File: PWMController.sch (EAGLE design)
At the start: 13 parts, among them IC1 LM555_DIP, Q1 BC337-25

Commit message: Adding updated files
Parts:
- D1, D2: value 1N4148 -> 1N4148DO35-7; device diode-1:1N4148 -> diode:1N4148DO35-7
- D3: device SparkFun-LED:LED5MM -> led:LED5MM
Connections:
- net GND: now also J1.2; no longer J1.1
- net N$1: now also J3.1; no longer J3.3
- net N$4: now also J3.3; no longer J3.1
- net VCC: now also J1.1; no longer J1.2
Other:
- moved on the sheet: J3
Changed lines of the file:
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@@
 <parts>
 <part name="C1" library="rcl" library_urn="urn:adsk.eagle:library:334" deviceset="CPOL-EU" device="E1.8-4" package3d_urn="urn:adsk.eagle:package:23336/2" value="2.2uF"/>
-<part name="IC1" library="IC_Clock-Timing" library_urn="urn:adsk.eagle:library:18568598" deviceset="*555" device="_DIP" package3d_urn="urn:adsk.eagle:package:18493555/1" technology="LM"/>
-<part name="D1" library="diode-1" deviceset="1N4148" device=""/>
-<part name="D2" library="diode-1" deviceset="1N4148" device=""/>
-<part name="D3" library="SparkFun-LED" library_urn="urn:adsk.eagle:library:529" deviceset="LED" device="5MM" package3d_urn="urn:adsk.eagle:package:39353/1"/>
+<part name="IC1" library="IC_Clock-Timing" library_urn="urn:adsk.eagle:library:18568598" deviceset="*555" device="_DIP" package3d_urn="urn:adsk.eagle:package:18493555/1" override_package3d_urn="urn:adsk.eagle:package:23438638/2" override_package_urn="urn:adsk.eagle:footprint:18493706/1" technology="LM"/>
+<part name="D1" library="diode" library_urn="urn:adsk.eagle:library:210" deviceset="1N4148" device="DO35-7" package3d_urn="urn:adsk.eagle:package:43339/2"/>
+<part name="D2" library="diode" library_urn="urn:adsk.eagle:library:210" deviceset="1N4148" device="DO35-7" package3d_urn="urn:adsk.eagle:package:43339/2"/>
+<part name="D3" library="led" library_urn="urn:adsk.eagle:library:259" deviceset="LED" device="5MM" package3d_urn="urn:adsk.eagle:package:15799/2"/>
 <part name="R2" library="rcl" library_urn="urn:adsk.eagle:library:334" deviceset="R-EU_" device="R1206" package3d_urn="urn:adsk.eagle:package:23540/2"/>
 <part name="C2" library="Capacitor" library_urn="urn:adsk.eagle:library:16290819" deviceset="C" device="CHIP-1206(3216-METRIC)" package3d_urn="urn:adsk.eagle:package:16290893/2" technology="_" value="10nF"/>
@@
 <attribute name="VALUE" x="185.42" y="71.12" size="1.778" layer="96"/>
 </instance>
-<instance part="GND2" gate="1" x="213.36" y="99.06" smashed="yes" grouprefs="POWER_TERMINALS">
-<attribute name="VALUE" x="210.82" y="96.52" size="1.778" layer="96"/>
-</instance>
-<instance part="P+2" gate="1" x="215.9" y="101.6" smashed="yes" rot="R180" grouprefs="POWER_TERMINALS">
-<attribute name="VALUE" x="218.44" y="101.6" size="1.778" layer="96"/>
+<instance part="GND2" gate="1" x="213.36" y="93.98" smashed="yes" grouprefs="POWER_TERMINALS">
+<attribute name="VALUE" x="210.82" y="91.44" size="1.778" layer="96"/>
+</instance>
+<instance part="P+2" gate="1" x="215.9" y="96.52" smashed="yes" rot="R180" grouprefs="POWER_TERMINALS">
+<attribute name="VALUE" x="218.44" y="96.52" size="1.778" layer="96"/>
 </instance>
 <instance part="P+1" gate="VCC" x="187.96" y="111.76" smashed="yes" grouprefs="POWER_TERMINALS">
@@
 <attribute name="VALUE" x="220.98" y="55.88" size="1.778" layer="96" rot="R180"/>
 </instance>
-<instance part="J3" gate="G$1" x="48.26" y="35.56" smashed="yes" rot="R90" grouprefs="DUTY_CYCLE_CIRCUITRY">
-<attribute name="NAME" x="49.182" y="30.68" size="1.016" layer="95" rot="R90" align="bottom-right"/>
-<attribute name="VALUE" x="50.84" y="30.73" size="1.016" layer="96" rot="R90" align="bottom-right"/>
+<instance part="J3" gate="G$1" x="48.26" y="35.56" smashed="yes" rot="MR270" grouprefs="DUTY_CYCLE_CIRCUITRY">
+<attribute name="NAME" x="49.182" y="40.44" size="1.016" layer="95" rot="MR270" align="bottom-right"/>
+<attribute name="VALUE" x="50.84" y="40.39" size="1.016" layer="96" rot="MR270" align="bottom-right"/>
 </instance>
 <instance part="R1" gate="G$1" x="134.62" y="40.64" smashed="yes" rot="R90" grouprefs="DUTY_CYCLE_CIRCUITRY">
@@
 <net name="V+" class="0">
 <segment>
-<pinref part="J2" gate="G$1" pin="2"/>
-<wire x1="215.9" y1="106.68" x2="215.9" y2="104.14" width="0.1524" layer="91" grouprefs="POWER_TERMINALS"/>
-<pinref part="P+2" gate="1" pin="V+"/>
-</segment>
-<segment>
 <pinref part="Q1" gate="G$1" pin="E"/>
 <wire x1="213.36" y1="33.02" x2="213.36" y2="25.4" width="0.1524" layer="91" grouprefs="OUTPUT_CIRCUITRY"/>
@@
 <wire x1="218.44" y1="25.4" x2="213.36" y2="25.4" width="0.1524" layer="91" grouprefs="OUTPUT_CIRCUITRY"/>
 </segment>
+<segment>
+<pinref part="P+2" gate="1" pin="V+"/>
+<pinref part="J2" gate="G$1" pin="2"/>
+<wire x1="215.9" y1="99.06" x2="215.9" y2="106.68" width="0.1524" layer="91"/>
+</segment>
 </net>
 <net name="GND" class="0">
 <segment>
 <pinref part="C3" gate="G$1" pin="-"/>
-<pinref part="J1" gate="G$1" pin="1"/>
-<wire x1="180.34" y1="106.68" x2="180.34" y2="96.52" width="0.1524" layer="91" grouprefs="POWER_TERMINALS"/>
-<wire x1="180.34" y1="96.52" x2="187.96" y2="96.52" width="0.1524" layer="91" grouprefs="POWER_TERMINALS"/>
+<wire x1="182.88" y1="96.52" x2="187.96" y2="96.52" width="0.1524" layer="91" grouprefs="POWER_TERMINALS"/>
 <wire x1="187.96" y1="96.52" x2="187.96" y2="76.2" width="0.1524" layer="91" grouprefs="POWER_TERMINALS"/>
 <junction x="187.96" y="96.52" grouprefs="POWER_TERMINALS"/>
 <pinref part="GND1" gate="1" pin="GND"/>
-</segment>
-<segment>
-<pinref part="GND2" gate="1" pin="GND"/>
-<pinref part="J2" gate="G$1" pin="1"/>
-<wire x1="213.36" y1="101.6" x2="213.36" y2="106.68" width="0.1524" layer="91" grouprefs="POWER_TERMINALS"/>
+<pinref part="J1" gate="G$1" pin="2"/>
+<wire x1="182.88" y1="106.68" x2="182.88" y2="96.52" width="0.1524" layer="91"/>
 </segment>
 <segment>
@@
 <pinref part="GND6" gate="1" pin="GND"/>
 </segment>
+<segment>
+<pinref part="GND2" gate="1" pin="GND"/>
+<pinref part="J2" gate="G$1" pin="1"/>
+<wire x1="213.36" y1="96.52" x2="213.36" y2="106.68" width="0.1524" layer="91"/>
+</segment>
 </net>
 <net name="VCC" class="0">
@@
 <wire x1="187.96" y1="104.14" x2="187.96" y2="109.22" width="0.1524" layer="91" grouprefs="POWER_TERMINALS"/>
 <pinref part="P+1" gate="VCC" pin="VCC"/>
-<pinref part="J1" gate="G$1" pin="2"/>
-<wire x1="182.88" y1="106.68" x2="182.88" y2="104.14" width="0.1524" layer="91" grouprefs="POWER_TERMINALS"/>
-<wire x1="182.88" y1="104.14" x2="187.96" y2="104.14" width="0.1524" layer="91" grouprefs="POWER_TERMINALS"/>
+<wire x1="180.34" y1="104.14" x2="187.96" y2="104.14" width="0.1524" layer="91" grouprefs="POWER_TERMINALS"/>
 <junction x="187.96" y="104.14" grouprefs="POWER_TERMINALS"/>
+<pinref part="J1" gate="G$1" pin="1"/>
+<wire x1="180.34" y1="104.14" x2="180.34" y2="106.68" width="0.1524" layer="91"/>
 </segment>
 <segment>
@@
 </segment>
 <segment>
+<pinref part="R1" gate="G$1" pin="1"/>
+<wire x1="134.62" y1="35.56" x2="147.32" y2="35.56" width="0.1524" layer="91" grouprefs="DUTY_CYCLE_CIRCUITRY"/>
+<label x="149.86" y="35.56" size="1.778" layer="95" grouprefs="DUTY_CYCLE_CIRCUITRY"/>
 <pinref part="J3" gate="G$1" pin="2"/>
-<pinref part="R1" gate="G$1" pin="1"/>
-<wire x1="53.34" y1="35.56" x2="134.62" y2="35.56" width="0.1524" layer="91" grouprefs="DUTY_CYCLE_CIRCUITRY"/>
-<wire x1="134.62" y1="35.56" x2="147.32" y2="35.56" width="0.1524" layer="91" grouprefs="DUTY_CYCLE_CIRCUITRY"/>
-<junction x="134.62" y="35.56" grouprefs="DUTY_CYCLE_CIRCUITRY"/>
-<label x="149.86" y="35.56" size="1.778" layer="95" grouprefs="DUTY_CYCLE_CIRCUITRY"/>
+<wire x1="53.34" y1="35.56" x2="134.62" y2="35.56" width="0.1524" layer="91"/>
+<junction x="134.62" y="35.56"/>
 </segment>
 </net>
 <net name="N$1" class="0">
 <segment>
-<pinref part="J3" gate="G$1" pin="3"/>
-<wire x1="53.34" y1="38.1" x2="63.5" y2="38.1" width="0.1524" layer="91" grouprefs="DUTY_CYCLE_CIRCUITRY"/>
-<wire x1="63.5" y1="38.1" x2="63.5" y2="43.18" width="0.1524" layer="91" grouprefs="DUTY_CYCLE_CIRCUITRY"/>
 <wire x1="63.5" y1="43.18" x2="76.2" y2="43.18" width="0.1524" layer="91" grouprefs="DUTY_CYCLE_CIRCUITRY"/>
 <pinref part="D1" gate="G$1" pin="A"/>
+<pinref part="J3" gate="G$1" pin="1"/>
+<wire x1="63.5" y1="43.18" x2="63.5" y2="38.1" width="0.1524" layer="91"/>
+<wire x1="63.5" y1="38.1" x2="53.34" y2="38.1" width="0.1524" layer="91"/>
 </segment>
 </net>
 <net name="N$4" class="0">
 <segment>
-<pinref part="J3" gate="G$1" pin="1"/>
-<wire x1="53.34" y1="33.02" x2="63.5" y2="33.02" width="0.1524" layer="91" grouprefs="DUTY_CYCLE_CIRCUITRY"/>
-<wire x1="63.5" y1="33.02" x2="63.5" y2="27.94" width="0.1524" layer="91" grouprefs="DUTY_CYCLE_CIRCUITRY"/>
 <wire x1="63.5" y1="27.94" x2="76.2" y2="27.94" width="0.1524" layer="91" grouprefs="DUTY_CYCLE_CIRCUITRY"/>
 <pinref part="D2" gate="G$1" pin="C"/>
+<pinref part="J3" gate="G$1" pin="3"/>
+<wire x1="53.34" y1="33.02" x2="63.5" y2="33.02" width="0.1524" layer="91"/>
+<wire x1="63.5" y1="33.02" x2="63.5" y2="27.94" width="0.1524" layer="91"/>
 </segment>
 </net>
@@
 will not be understood (or retained) with this version.
 </note>
+<note version="9.4" severity="warning">
+Since Version 9.4, EAGLE supports the overriding of 3D packages
+in schematics and board files. Those overridden 3d packages
+will not be understood (or retained) with this version.
+</note>

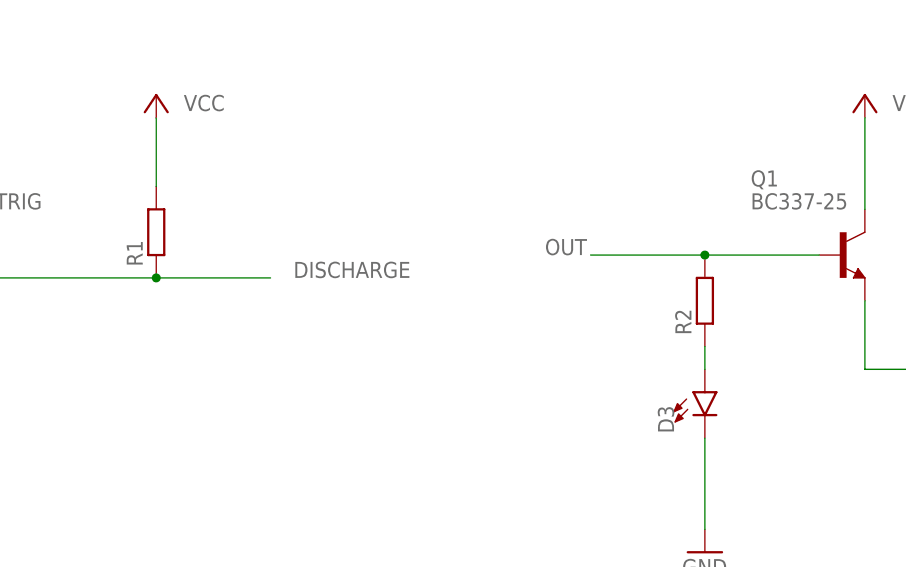
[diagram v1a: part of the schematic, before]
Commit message: Adding Schematic components update and populated PCB pictures
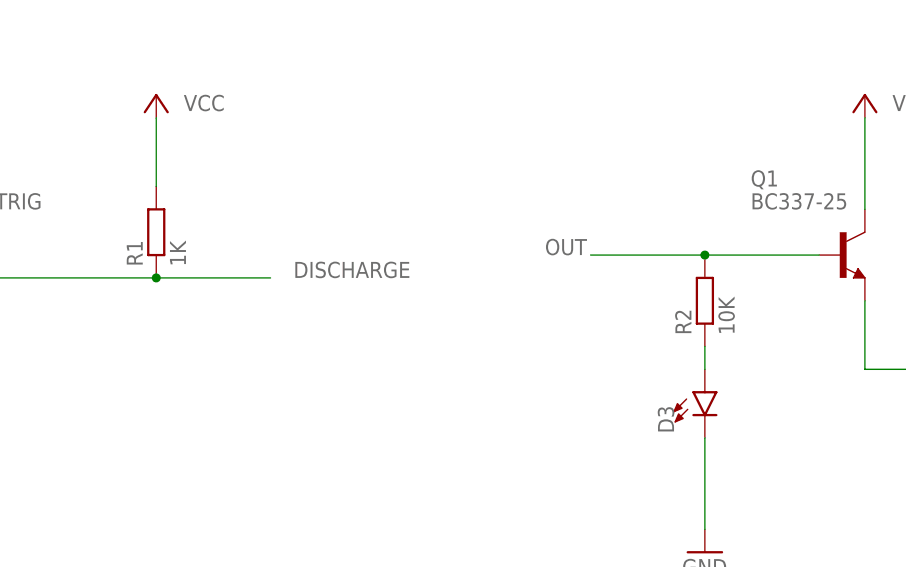
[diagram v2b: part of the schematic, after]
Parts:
- C3: value XmF -> 100mF
- R1: value (none) -> 1K
- R2: value (none) -> 10K
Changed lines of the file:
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@@
 <part name="D2" library="diode" library_urn="urn:adsk.eagle:library:210" deviceset="1N4148" device="DO35-7" package3d_urn="urn:adsk.eagle:package:43339/2"/>
 <part name="D3" library="led" library_urn="urn:adsk.eagle:library:259" deviceset="LED" device="5MM" package3d_urn="urn:adsk.eagle:package:15799/2"/>
-<part name="R2" library="rcl" library_urn="urn:adsk.eagle:library:334" deviceset="R-EU_" device="R1206" package3d_urn="urn:adsk.eagle:package:23540/2"/>
+<part name="R2" library="rcl" library_urn="urn:adsk.eagle:library:334" deviceset="R-EU_" device="R1206" package3d_urn="urn:adsk.eagle:package:23540/2" value="10K"/>
 <part name="C2" library="Capacitor" library_urn="urn:adsk.eagle:library:16290819" deviceset="C" device="CHIP-1206(3216-METRIC)" package3d_urn="urn:adsk.eagle:package:16290893/2" technology="_" value="10nF"/>
 <part name="Q1" library="transistor-npn" library_urn="urn:adsk.eagle:library:398" deviceset="BC337*" device="" package3d_urn="urn:adsk.eagle:package:28523/2" technology="-25"/>
 <part name="J1" library="Wurth_Connectors_WR-TBL Rising Cage Clamp" library_urn="urn:adsk.eagle:library:16280519" deviceset="691213510002" device="" package3d_urn="urn:adsk.eagle:package:16248575/2"/>
 <part name="J2" library="Wurth_Connectors_WR-TBL Rising Cage Clamp" library_urn="urn:adsk.eagle:library:16280519" deviceset="691213510002" device="" package3d_urn="urn:adsk.eagle:package:16248575/2"/>
-<part name="C3" library="rcl" library_urn="urn:adsk.eagle:library:334" deviceset="CPOL-EU" device="E1.8-4" package3d_urn="urn:adsk.eagle:package:23336/2" value="XmF"/>
+<part name="C3" library="rcl" library_urn="urn:adsk.eagle:library:334" deviceset="CPOL-EU" device="E1.8-4" package3d_urn="urn:adsk.eagle:package:23336/2" value="100mF"/>
 <part name="GND1" library="supply1" library_urn="urn:adsk.eagle:library:371" deviceset="GND" device=""/>
 <part name="GND2" library="supply1" library_urn="urn:adsk.eagle:library:371" deviceset="GND" device=""/>
@@
 <part name="P+5" library="supply1" library_urn="urn:adsk.eagle:library:371" deviceset="VCC" device=""/>
 <part name="J3" library="Wurth_Connectors_WR-TBL Rising Cage Clamp" library_urn="urn:adsk.eagle:library:16280519" deviceset="691213510003" device="" package3d_urn="urn:adsk.eagle:package:16248576/2"/>
-<part name="R1" library="rcl" library_urn="urn:adsk.eagle:library:334" deviceset="R-EU_" device="R1206" package3d_urn="urn:adsk.eagle:package:23540/2"/>
+<part name="R1" library="rcl" library_urn="urn:adsk.eagle:library:334" deviceset="R-EU_" device="R1206" package3d_urn="urn:adsk.eagle:package:23540/2" value="1K"/>
 <part name="P+7" library="supply1" library_urn="urn:adsk.eagle:library:371" deviceset="VCC" device=""/>
 <part name="GND6" library="supply1" library_urn="urn:adsk.eagle:library:371" deviceset="GND" device=""/>
